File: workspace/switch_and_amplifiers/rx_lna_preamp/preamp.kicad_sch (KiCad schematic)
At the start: 23 parts, among them J1 RF_IN, J2 RF_OUT, J3 Power, U1 PHA-13LN, U2 7805

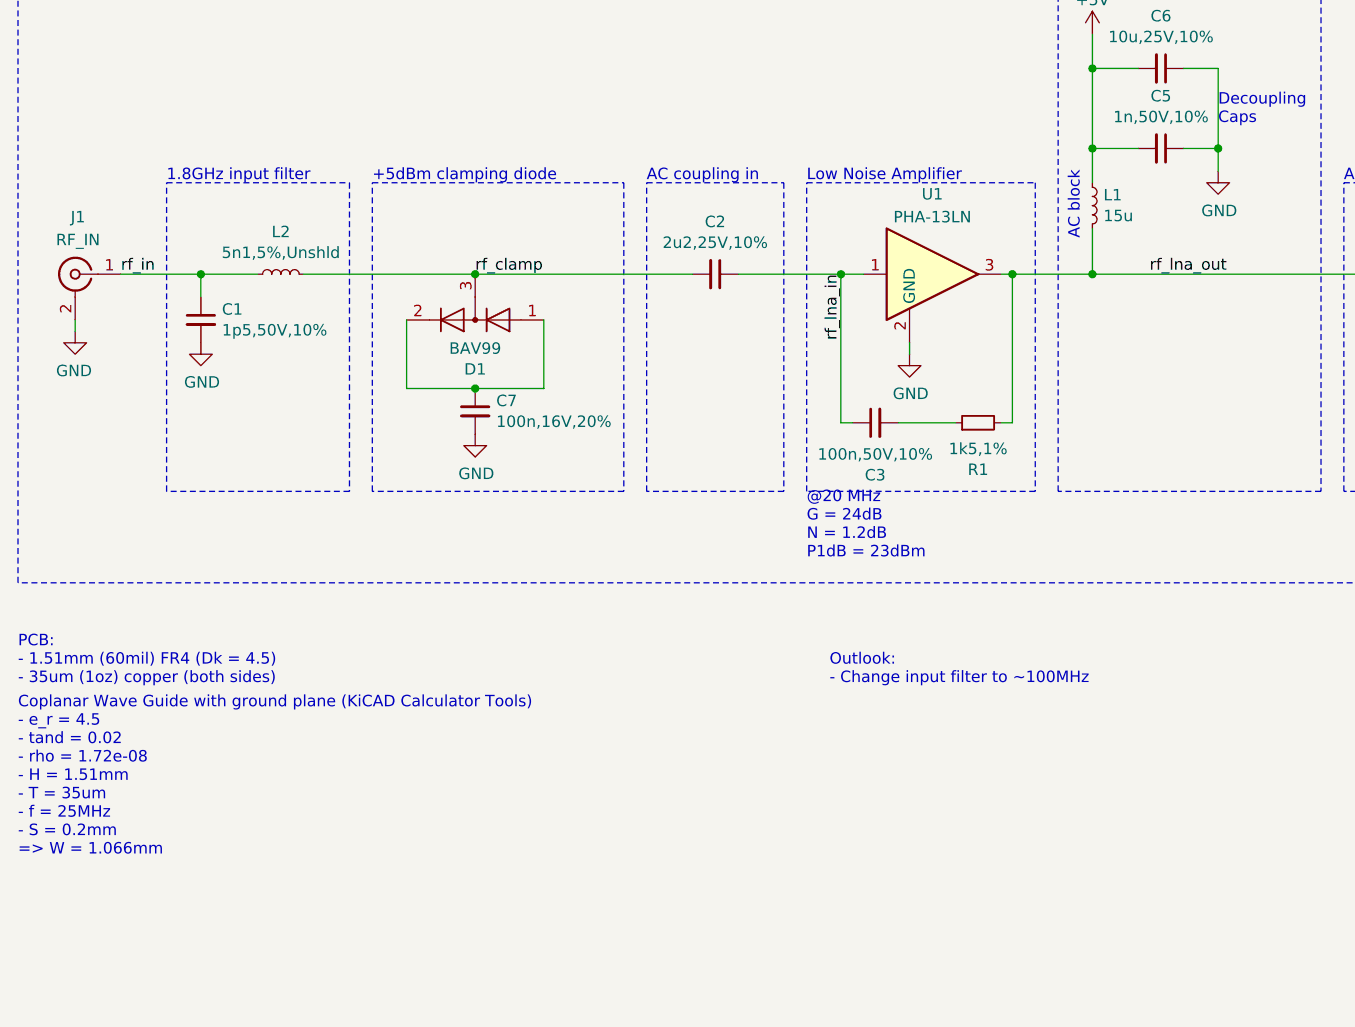
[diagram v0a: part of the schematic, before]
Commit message: Order at JLCPCB with modified rf clearances
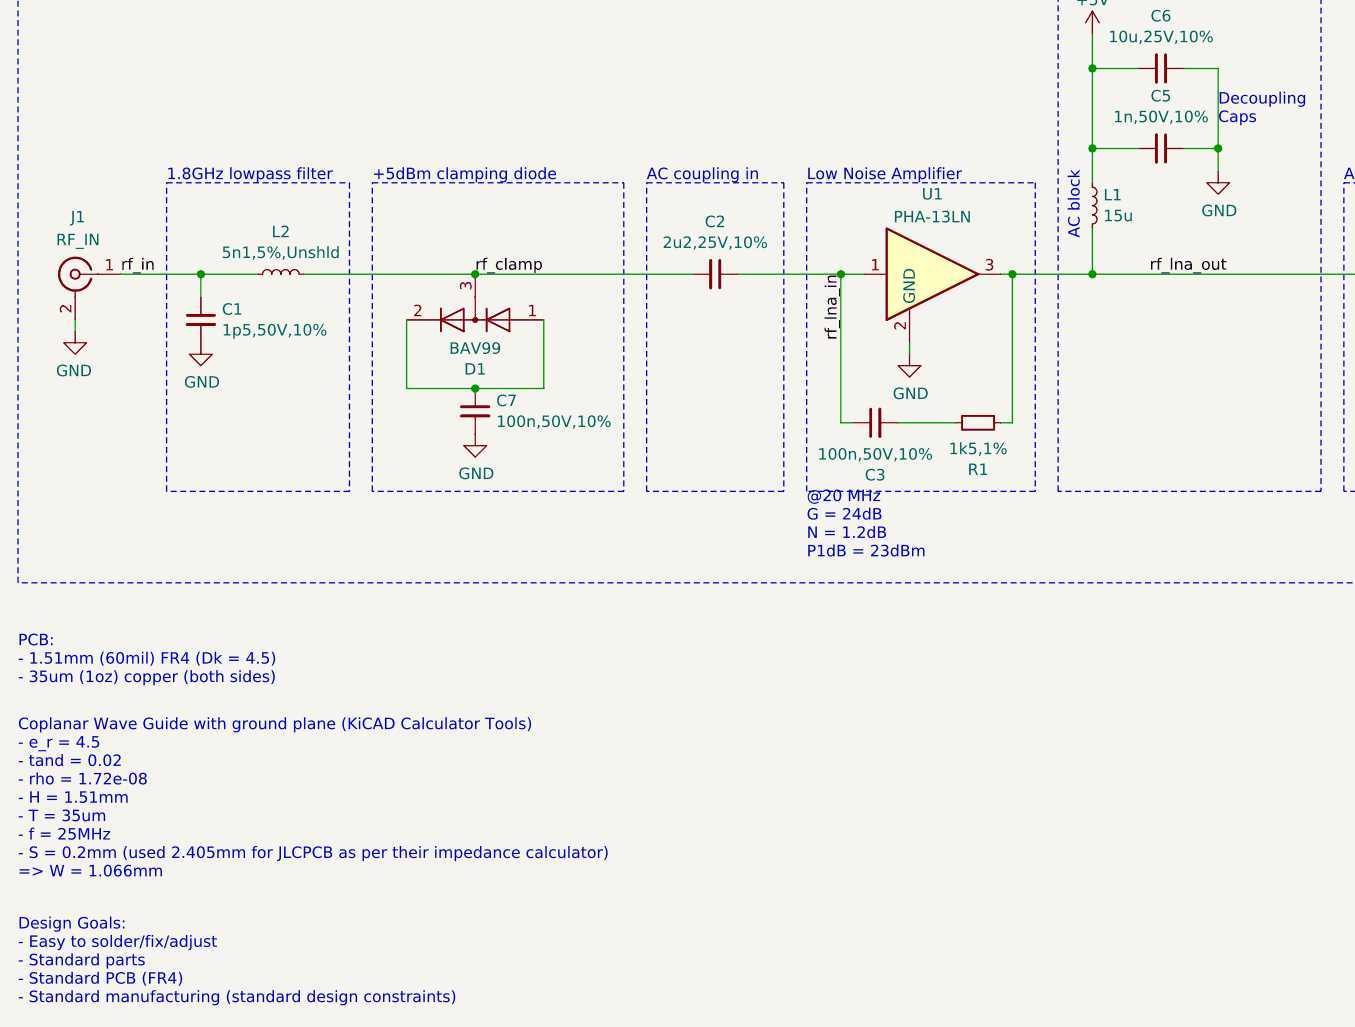
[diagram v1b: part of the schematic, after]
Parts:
- C7: value 100n,16V,20% -> 100n,50V,10%; DigiKey 587-EMF105B7104MVHFCT-ND -> (none); MPN EMF105B7104MVHF -> CL21B104KBCNNNC; Mouser 963-EMF105B7104MVHF -> 187-CL21B104KBCNNNC
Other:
- note added: "1.8GHz lowpass filter"
- note added: "Coplanar Wave Guide with ground plane (KiCAD Calculator Tools) - e_r = 4.5 - tand = 0.02 - rho = 1.72e-08 - H = 1.51mm - T = 35um - f = 25MHz - S = 0.2mm (used 2.405mm for JLCPCB as per their impedance calculator) => W = 1.066mm"
- note added: "Design Goals: - Easy to solder/fix/adjust - Standard parts - Standard PCB (FR4) - Standard manufacturing (standard design constraints)"
- note removed: "1.8GHz input filter"
- note removed: "Coplanar Wave Guide with ground plane (KiCAD Calculator Tools) - e_r = 4.5 - tand = 0.02 - rho = 1.72e-08 - H = 1.51mm - T = 35um - f = 25MHz - S = 0.2mm => W = 1.066mm"
- note removed: "Outlook: - Change input filter to ~100MHz"
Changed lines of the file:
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@@
     (fill (type none))
+  )
+  (text "Design Goals:\n- Easy to solder/fix/adjust\n- Standard parts\n- Standard PCB (FR4)\n- Standard manufacturing (standard design constraints)"
+    (at 45.72 190.5 0)
+    (effects (font (size 1.27 1.27)) (justify left bottom))
   )
   (text "Amplifier 50Ohm, 1MHz..1GHz" (at 45.72 69.85 0)
@@
     (effects (font (size 2.54 2.54)) (justify left bottom))
   )
-  (text "Outlook:\n- Change input filter to ~100MHz" (at 135.89 154.94 0)
-    (effects (font (size 1.27 1.27)) (justify left bottom))
-  )
   (text "AC coupling out" (at 193.04 99.06 0)
     (effects (font (size 1.27 1.27)) (justify left bottom))
   )
-  (text "1.8GHz input filter" (at 62.23 99.06 0)
+  (text "1.8GHz lowpass filter" (at 62.23 99.06 0)
     (effects (font (size 1.27 1.27)) (justify left bottom))
   )
@@
     (effects (font (size 1.27 1.27)) (justify left bottom))
   )
-  (text "Coplanar Wave Guide with ground plane (KiCAD Calculator Tools)\n- e_r = 4.5\n- tand = 0.02\n- rho = 1.72e-08\n- H = 1.51mm\n- T = 35um\n- f = 25MHz\n- S = 0.2mm\n=> W = 1.066mm"
-    (at 45.72 173.99 0)
+  (text "Coplanar Wave Guide with ground plane (KiCAD Calculator Tools)\n- e_r = 4.5\n- tand = 0.02\n- rho = 1.72e-08\n- H = 1.51mm\n- T = 35um\n- f = 25MHz\n- S = 0.2mm (used 2.405mm for JLCPCB as per their impedance calculator)\n=> W = 1.066mm"
+    (at 45.72 176.53 0)
     (effects (font (size 1.27 1.27)) (justify left bottom))
   )
@@
       (effects (font (size 1.27 1.27)) (justify left))
     )
-    (property "Value" "100n,16V,20%" (at 98.8568 125.603 0)
+    (property "Value" "100n,50V,10%" (at 98.8568 125.603 0)
       (effects (font (size 1.27 1.27)) (justify left))
     )
@@
       (effects (font (size 1.27 1.27)) hide)
     )
-    (property "Datasheet" "https://media.digikey.com/pdf/Data%20Sheets/Taiyo%20Yuden%20PDFs%20URL%20links/EMF105B7104MVHF_SS.pdf" (at 96.52 124.46 0)
-      (effects (font (size 1.27 1.27)) hide)
-    )
-    (property "MPN" "EMF105B7104MVHF " (at 96.52 124.46 0)
-      (effects (font (size 1.27 1.27)) hide)
-    )
-    (property "Mouser" "963-EMF105B7104MVHF " (at 96.52 124.46 0)
-      (effects (font (size 1.27 1.27)) hide)
-    )
-    (property "DigiKey" "587-EMF105B7104MVHFCT-ND" (at 96.52 124.46 0)
-      (effects (font (size 1.27 1.27)) hide)
-    )
+    (property "Datasheet" "https://www.mouser.ch/datasheet/2/585/MLCC-1837944.pdf" (at 96.52 124.46 0)
+      (effects (font (size 1.27 1.27)) hide)
+    )
+    (property "MPN" "CL21B104KBCNNNC" (at 96.52 124.46 0)
+      (effects (font (size 1.27 1.27)) hide)
+    )
+    (property "Mouser" "187-CL21B104KBCNNNC" (at 96.52 124.46 0)
+      (effects (font (size 1.27 1.27)) hide)
+    )
+    (property "DigiKey" "" (at 96.52 124.46 0)
+      (effects (font (size 1.27 1.27)) hide)
+    )
